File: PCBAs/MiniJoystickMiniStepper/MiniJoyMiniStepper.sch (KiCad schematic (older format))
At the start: 54 parts, among them J0 STEPPER_UNI_5P, J1 STEPPER_UNI_5P, J10 TH_0.1_1x1, J100 TH_0.1_1x1, J101 TH_0.1_1x1, J102 TH_0.1_1x1, J103 TH_0.1_1x1, J104 TH_0.1_1x1, J105 TH_0.1_1x1, J107 TH_0.1_1x1, J11 TH_0.1_1x1, J12 TH_0.1_1x1, J13 TH_0.1_1x1, J14 TH_0.1_1x1, J15 TH_0.1_1x1, J16 TH_0.1_1x1, J2 STEPPER_UNI_5P, J3 STEPPER_UNI_5P, J4 STEPPER_UNI_5P, J5 STEPPER_UNI_5P, J6 STEPPER_UNI_5P, J7 STEPPER_UNI_5P, J8 TH_0.1_1x1, J9 TH_0.1_1x1, U1 MCP3008T-I/SL, U10 ULN2803, U11 STM32F103C8T6_BLUE_PILL, U2 OLED_128x32_I2C, U3 CD74HC595, U4 CD74HC595, U5 CD74HC595, U6 CD74HC595, U7 ULN2803, U8 ULN2803, U9 ULN2803

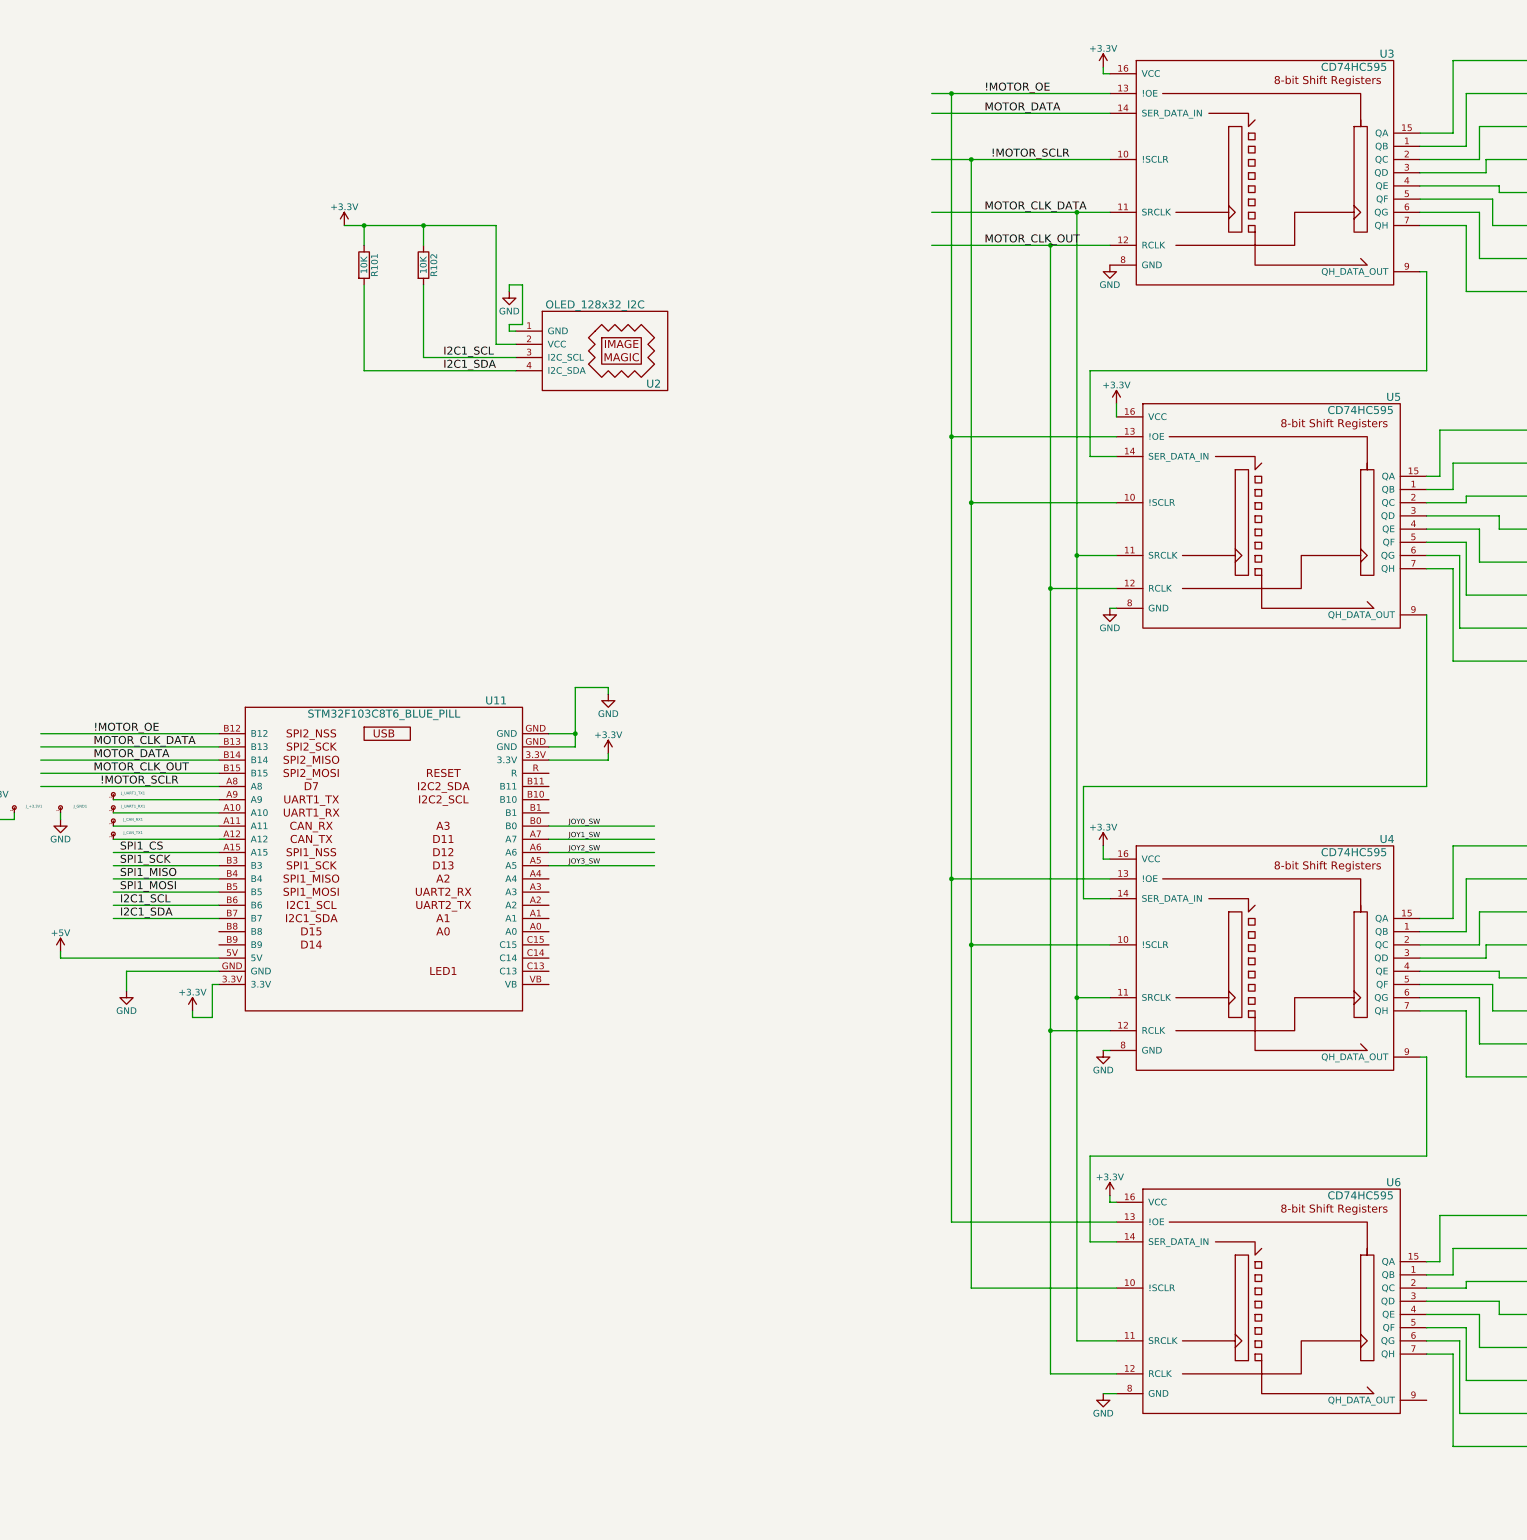
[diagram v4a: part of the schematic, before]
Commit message: Added 0.1" header for daisy chaining shift register / motor driver.
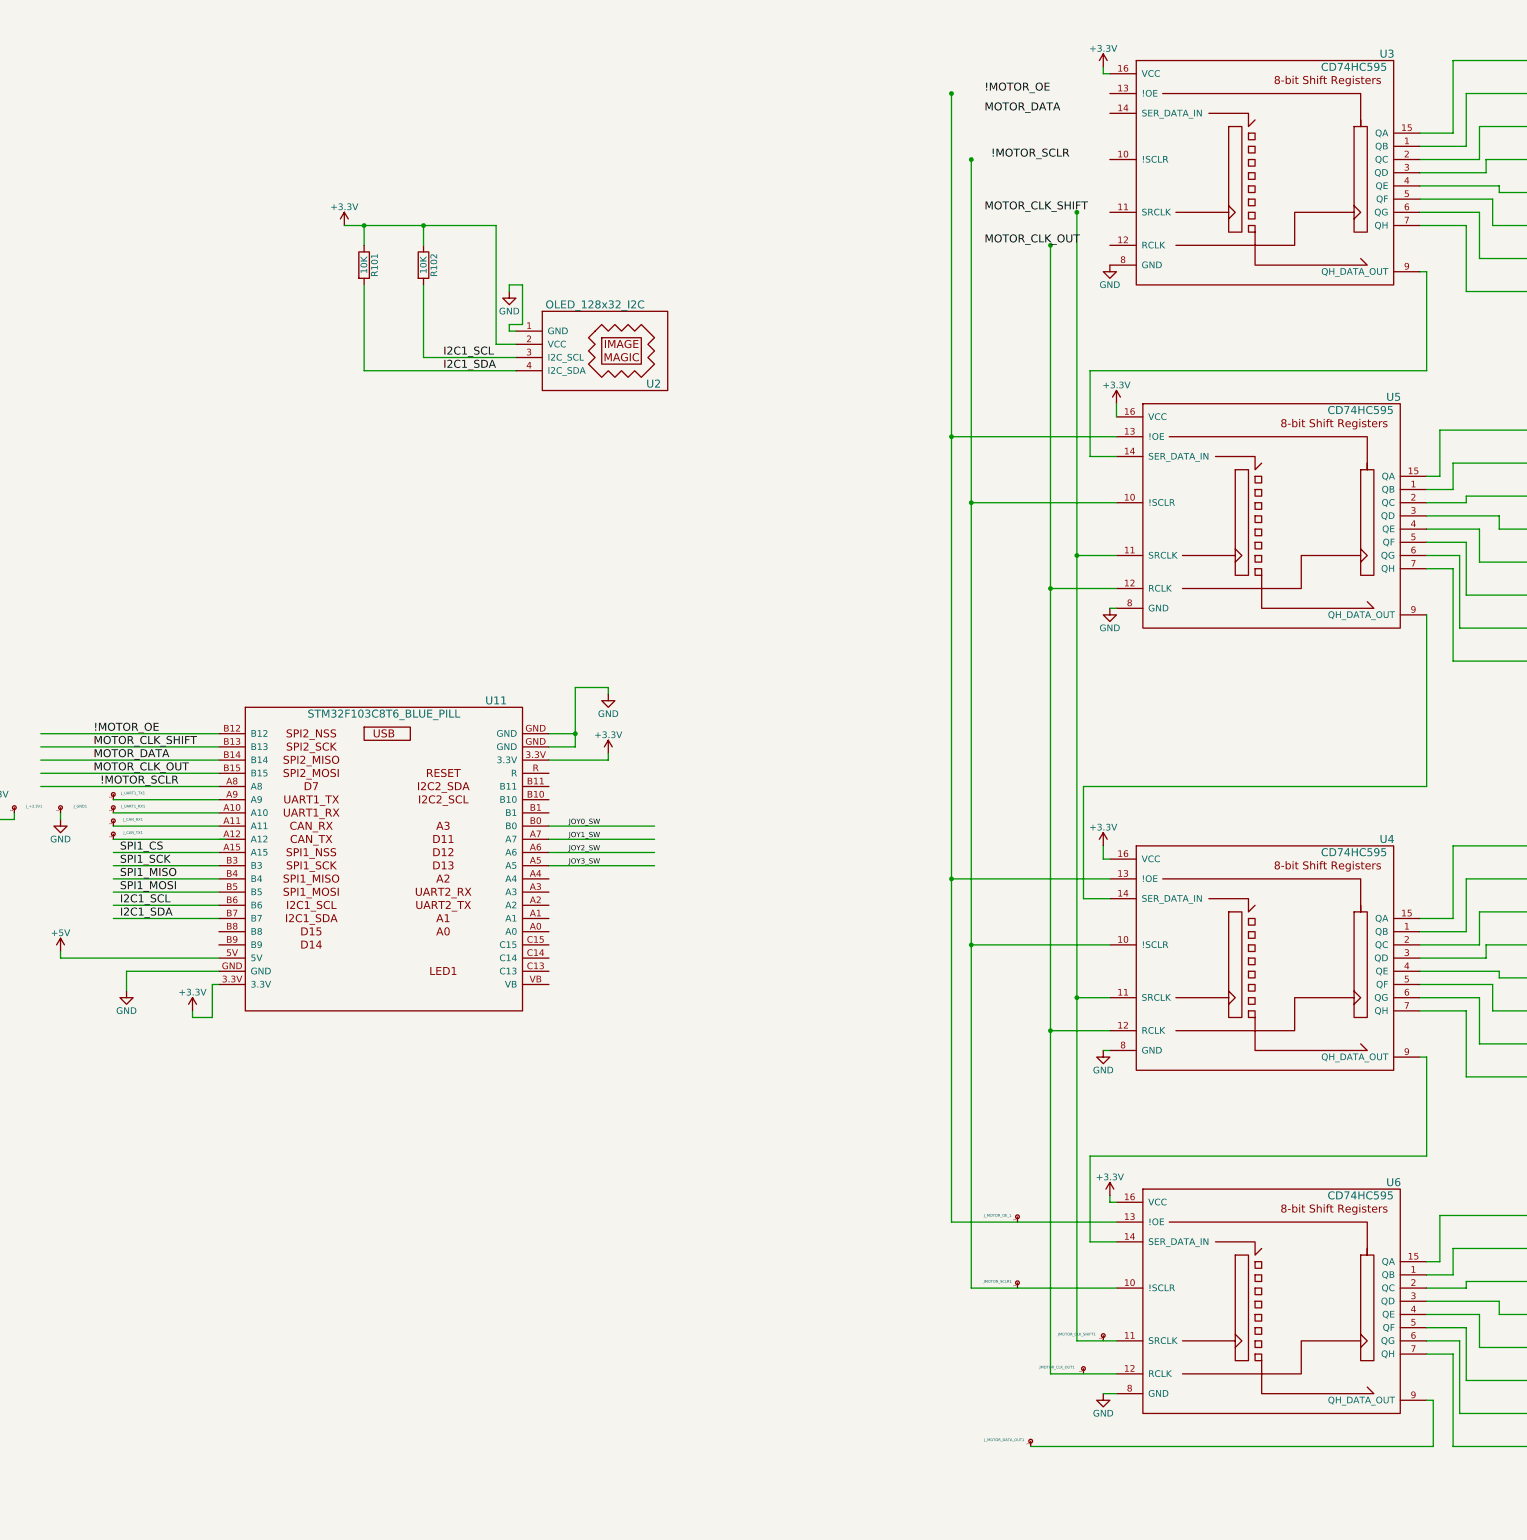
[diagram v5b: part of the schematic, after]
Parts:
- added JMOTOR_CLK_OUT1, JMOTOR_CLK_SHIFT1, JMOTOR_SCLR1, J_MOTOR_DATA_OUT1, J_MOTOR_OE_1: TH_0.1_1x1, Liberry:single_0.1, symbol TH_0.1_1x1
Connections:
- net labels added: MOTOR_CLK_SHIFT
- net labels removed: MOTOR_CLK_DATA
- wire segments 391 -> 389
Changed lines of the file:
@@
 $EndComp
 Text Label 15350 2300 0    60   ~ 0
-MOTOR_CLK_DATA
+MOTOR_CLK_SHIFT
 $Comp
 L GND #PWR010
@@
 	16050 10850 16350 10850
 Connection ~ 16050 8250
-Wire Wire Line
-	14950 2300 16300 2300
 Connection ~ 16050 2300
-Wire Wire Line
-	14950 2550 16300 2550
 Wire Wire Line
 	16350 11250 16250 11250
@@
 Connection ~ 15850 8500
 Wire Wire Line
-	16300 1550 14950 1550
-Wire Wire Line
-	14950 1400 16300 1400
-Wire Wire Line
 	15100 1400 15100 9950
 Wire Wire Line
@@
 	15100 9950 16350 9950
 Connection ~ 15100 7350
-Wire Wire Line
-	14950 1900 16300 1900
 Wire Wire Line
 	15250 1900 15250 10450
@@
 $EndComp
 Text Label 8600 6350 0    60   ~ 0
-MOTOR_CLK_DATA
+MOTOR_CLK_SHIFT
 Text Label 8600 6450 0    60   ~ 0
 MOTOR_DATA
@@
 	1200 2500 1200 2450
 Connection ~ 1200 2450
+$Comp
+L TH_0.1_1x1 J_MOTOR_OE_1
+U 1 1 5A91B2F0
+P 15600 9950
+F 0 "J_MOTOR_OE_1" H 15450 10000 20  0000 C CNN
+F 1 "TH_0.1_1x1" H 15600 9950 60  0001 C CNN
+F 2 "Liberry:single_0.1" H 15600 9950 60  0001 C CNN
+F 3 "" H 15600 9950 60  0001 C CNN
+	1    15600 9950
+	1    0    0    -1
+$EndComp
+$Comp
+L TH_0.1_1x1 J_MOTOR_DATA_OUT1
+U 1 1 5A91C126
+P 15700 11650
+F 0 "J_MOTOR_DATA_OUT1" H 15500 11700 20  0000 C CNN
+F 1 "TH_0.1_1x1" H 15700 11650 60  0001 C CNN
+F 2 "Liberry:single_0.1" H 15700 11650 60  0001 C CNN
+F 3 "" H 15700 11650 60  0001 C CNN
+	1    15700 11650
+	1    0    0    -1
+$EndComp
+$Comp
+L TH_0.1_1x1 JMOTOR_SCLR1
+U 1 1 5A91C1E4
+P 15600 10450
+F 0 "JMOTOR_SCLR1" H 15450 10500 20  0000 C CNN
+F 1 "TH_0.1_1x1" H 15600 10450 60  0001 C CNN
+F 2 "Liberry:single_0.1" H 15600 10450 60  0001 C CNN
+F 3 "" H 15600 10450 60  0001 C CNN
+	1    15600 10450
+	1    0    0    -1
+$EndComp
+$Comp
+L TH_0.1_1x1 JMOTOR_CLK_SHIFT1
+U 1 1 5A91C2A9
+P 16250 10850
+F 0 "JMOTOR_CLK_SHIFT1" H 16050 10900 20  0000 C CNN
+F 1 "TH_0.1_1x1" H 16250 10850 60  0001 C CNN
+F 2 "Liberry:single_0.1" H 16250 10850 60  0001 C CNN
+F 3 "" H 16250 10850 60  0001 C CNN
+	1    16250 10850
+	1    0    0    -1
+$EndComp
+$Comp
+L TH_0.1_1x1 JMOTOR_CLK_OUT1
+U 1 1 5A91CDDD
+P 16100 11100
+F 0 "JMOTOR_CLK_OUT1" H 15900 11150 20  0000 C CNN
+F 1 "TH_0.1_1x1" H 16100 11100 60  0001 C CNN
+F 2 "Liberry:single_0.1" H 16100 11100 60  0001 C CNN
+F 3 "" H 16100 11100 60  0001 C CNN
+	1    16100 11100
+	1    0    0    -1
+$EndComp
+Wire Wire Line
+	18700 11300 18750 11300
+Wire Wire Line
+	18750 11300 18750 11650
+Wire Wire Line
+	18750 11650 15700 11650
 $EndSCHEMATC

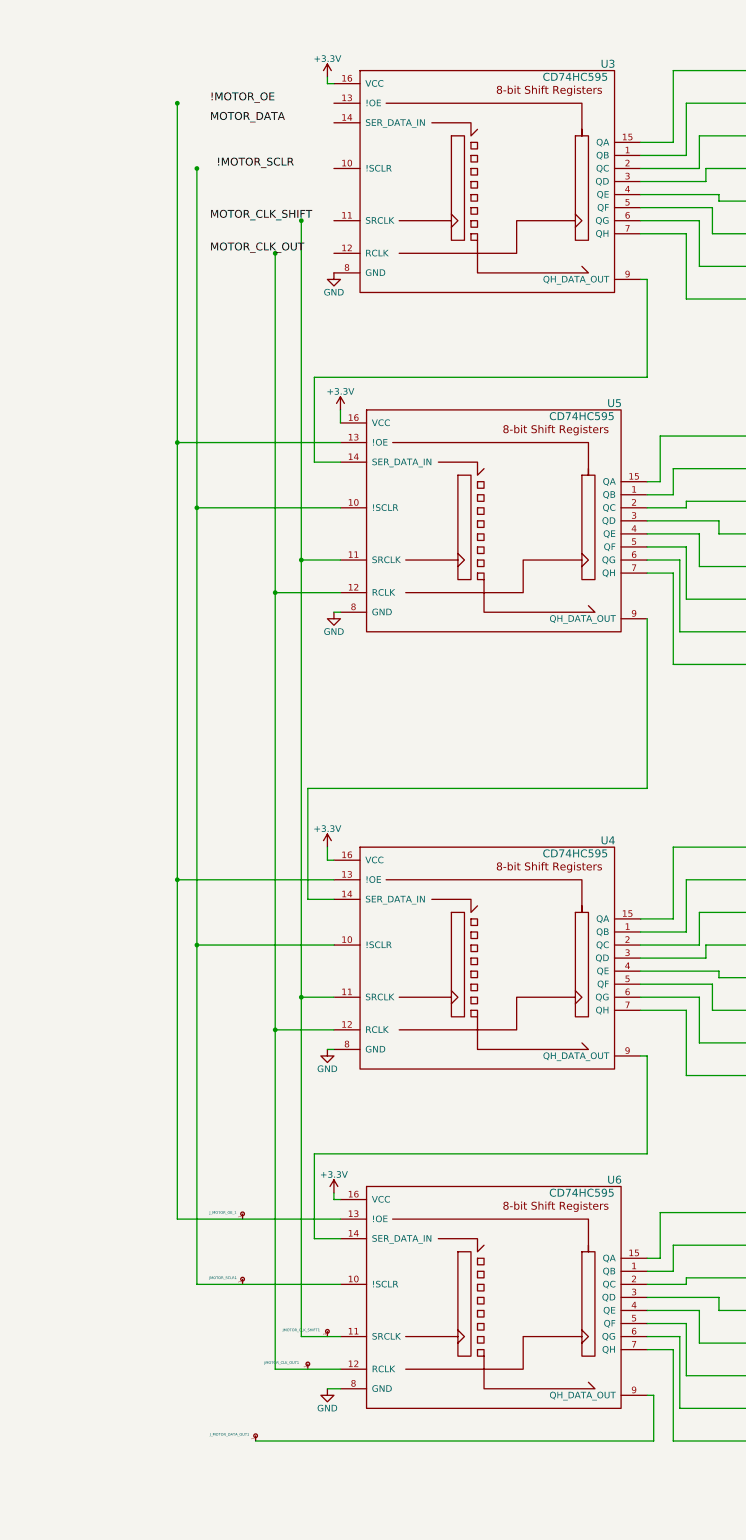
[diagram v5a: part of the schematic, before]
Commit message: Replaced cut copy instead of copy paste accident. Added GND + VCC pins
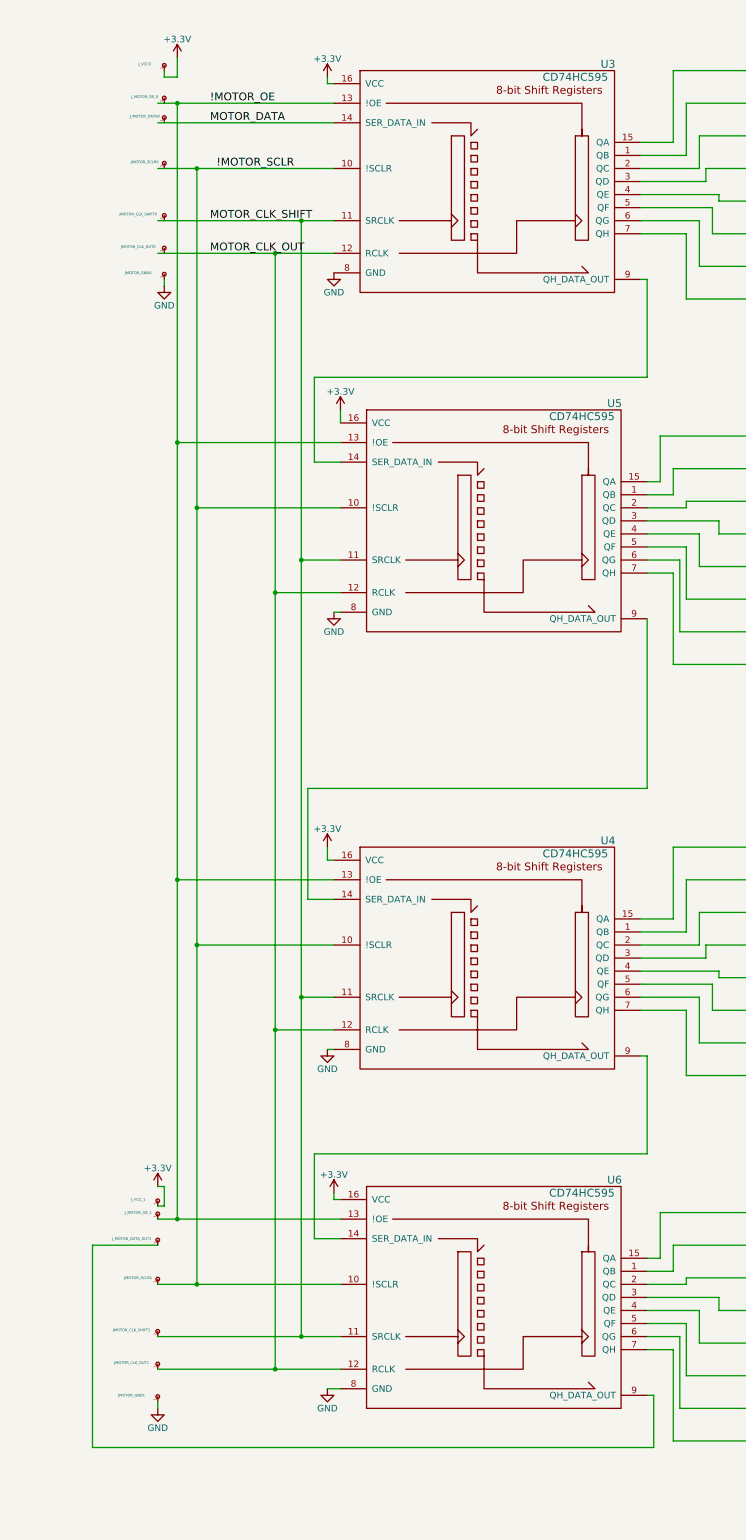
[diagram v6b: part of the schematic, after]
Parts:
- added JMOTOR_CLK_OUT1, JMOTOR_CLK_SHIFT1, JMOTOR_GND0, JMOTOR_GND1, JMOTOR_SCLR1, J_MOTOR_DATA_OUT1, J_MOTOR_OE_1, J_VCC0, J_VCC_1: TH_0.1_1x1, Liberry:single_0.1, symbol TH_0.1_1x1
- renumbered JMOTOR_CLK_OUT1 to JMOTOR_CLK_OUT0, JMOTOR_CLK_SHIFT1 to JMOTOR_CLK_SHIFT0, JMOTOR_SCLR1 to JMOTOR_SCLR0, J_MOTOR_DATA_OUT1 to J_MOTOR_DATA0, J_MOTOR_OE_1 to J_MOTOR_OE_0
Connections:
- wire segments 389 -> 404
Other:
- moved on the sheet: JMOTOR_CLK_OUT0, JMOTOR_CLK_SHIFT0, JMOTOR_SCLR0, J_MOTOR_DATA0, J_MOTOR_OE_0

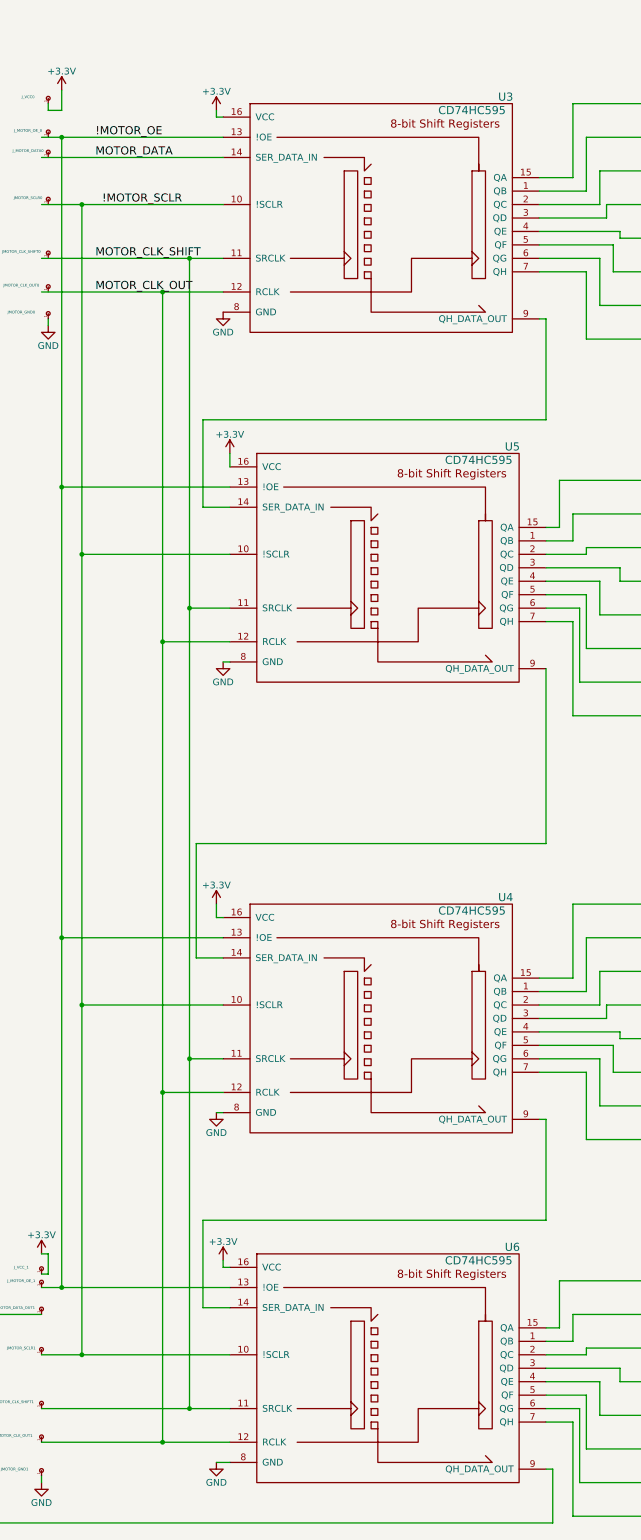
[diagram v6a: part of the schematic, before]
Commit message: Added bypass caps to Shift Registers.
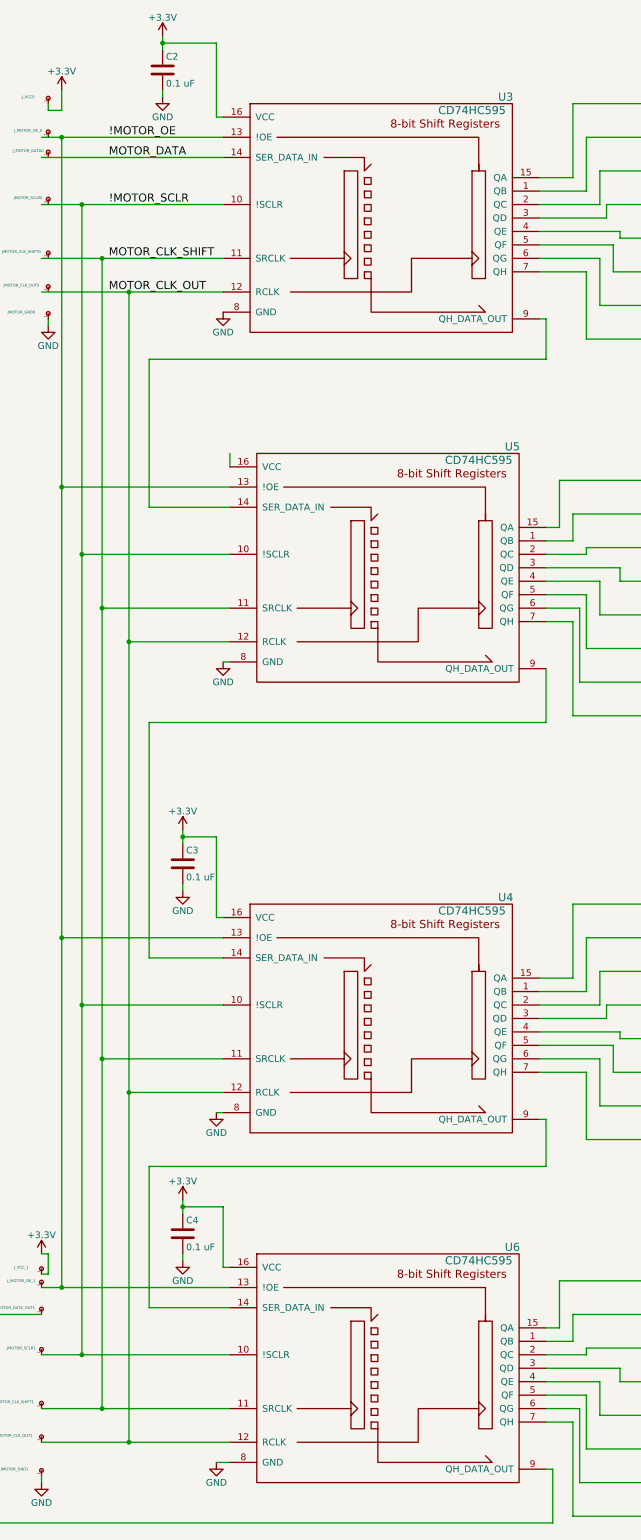
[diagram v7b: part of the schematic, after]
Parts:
- added C2, C3, C4: 0.1 uF, Capacitors_SMD:C_0603, symbol C
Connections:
- wire segments 404 -> 413
